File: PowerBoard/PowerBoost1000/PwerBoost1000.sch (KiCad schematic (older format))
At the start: 23 parts, among them T401 MMUN2133LT1G, U401 TPS61030RSAR

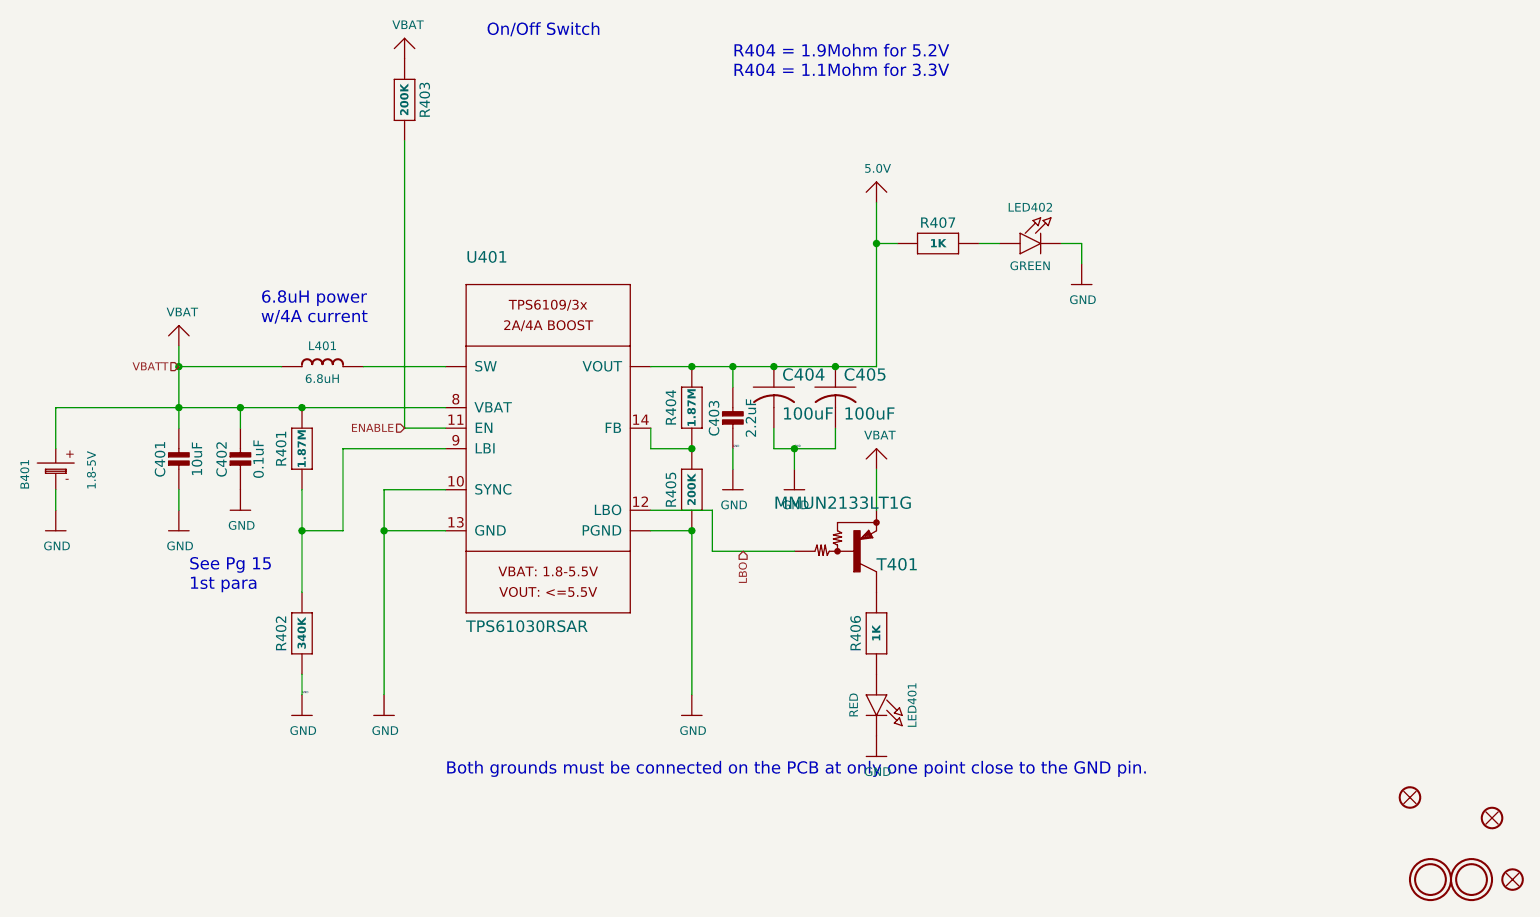
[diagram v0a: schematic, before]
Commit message: Replacing the SEPIC converter.
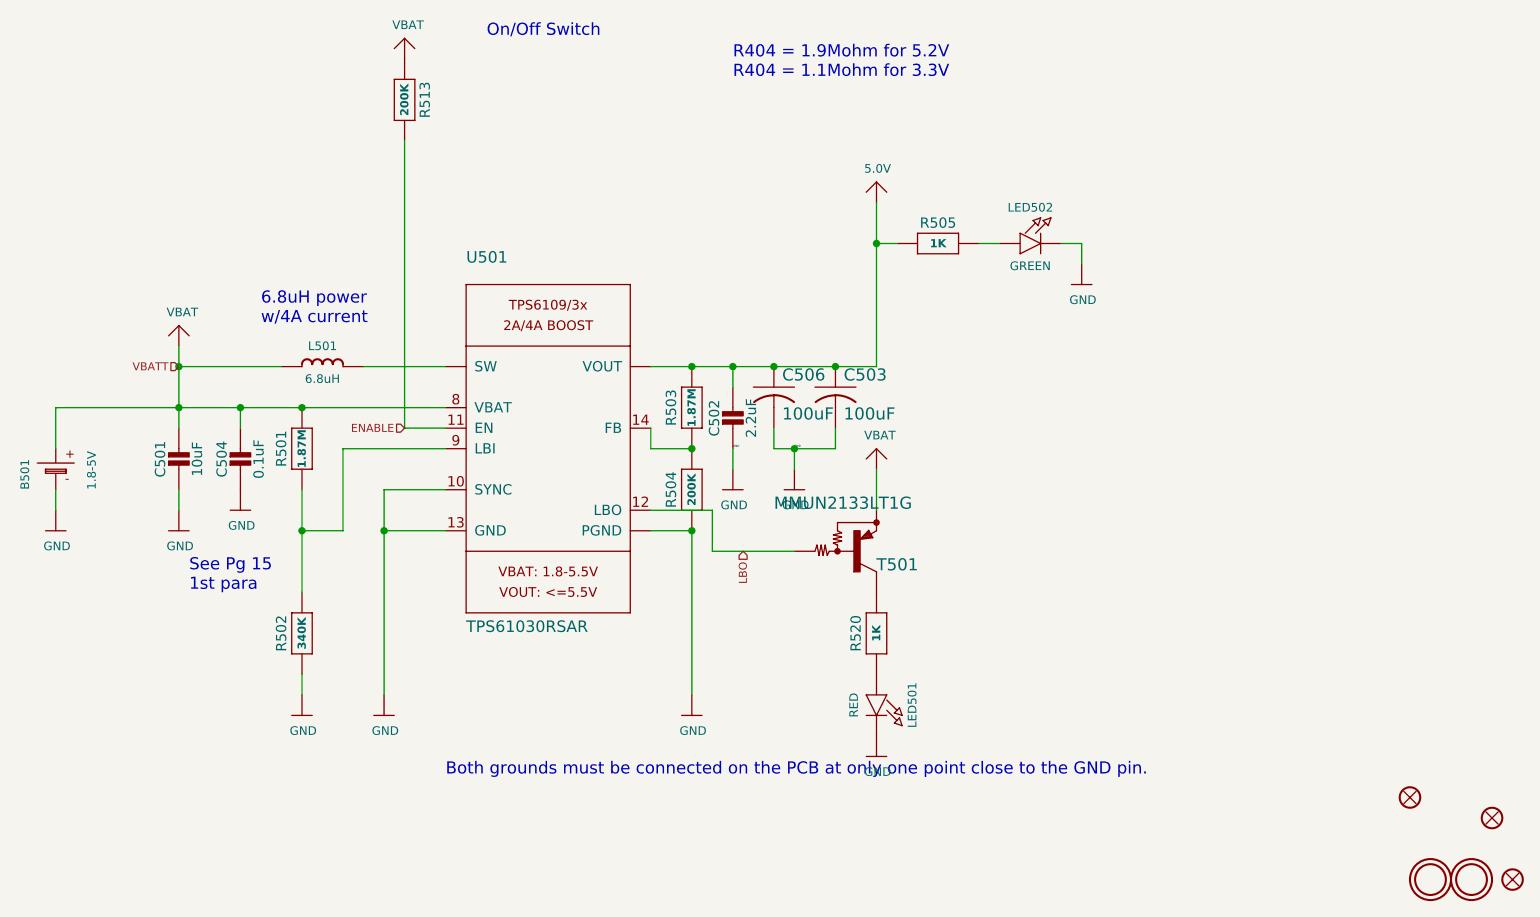
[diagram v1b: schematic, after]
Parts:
- C501: renamed from C401; footprint PowerBoost1000:0805-NO -> Capacitor_SMD:C_0805_2012Metric_Pad1.15x1.40mm_HandSolder
- C502: renamed from C403; footprint PowerBoost1000:0805-NO -> Capacitor_SMD:C_0805_2012Metric_Pad1.15x1.40mm_HandSolder
- C503: renamed from C405; footprint PowerBoost1000:C1210 -> Capacitor_SMD:C_1210_3225Metric_Pad1.42x2.65mm_HandSolder
- C504: renamed from C402; footprint PowerBoost1000:0805-NO -> Capacitor_SMD:C_0805_2012Metric_Pad1.15x1.40mm_HandSolder
- C506: renamed from C404; footprint PowerBoost1000:C1210 -> Capacitor_SMD:C_1210_3225Metric_Pad1.42x2.65mm_HandSolder
- R502: renamed from R402; footprint PowerBoost1000:_0805MP -> Resistor_SMD:R_0805_2012Metric_Pad1.15x1.40mm_HandSolder
- R503: renamed from R404; footprint PowerBoost1000:_0805MP -> Resistor_SMD:R_0805_2012Metric_Pad1.15x1.40mm_HandSolder
- R504: renamed from R405; footprint PowerBoost1000:0805-NO -> Resistor_SMD:R_0805_2012Metric_Pad1.15x1.40mm_HandSolder
- R505: renamed from R407; footprint PowerBoost1000:0805-NO -> Resistor_SMD:R_0805_2012Metric_Pad1.15x1.40mm_HandSolder
- R513: renamed from R403; footprint PowerBoost1000:0805-NO -> Resistor_SMD:R_0805_2012Metric_Pad1.15x1.40mm_HandSolder
- R520: renamed from R406; footprint PowerBoost1000:0805-NO -> Resistor_SMD:R_0805_2012Metric_Pad1.15x1.40mm_HandSolder
- U$501: renamed from U$401; footprint PowerBoost1000:MOUNTINGHOLE_2.5_PLATED -> MountingHole:MountingHole_2.5mm_Pad
- U$502: renamed from U$402; footprint PowerBoost1000:MOUNTINGHOLE_2.5_PLATED -> MountingHole:MountingHole_2.5mm_Pad
- U501: renamed from U401; footprint PowerBoost1000:PVQFN-16 -> Package_DFN_QFN:Texas_S-PVQFN-N16_EP2.7x2.7mm_ThermalVias
- renumbered B401 to B501, FID401 to FID501, FID402 to FID502, FID403 to FID503, L401 to L501, LED401 to LED501, LED402 to LED502, R401 to R501, T401 to T501
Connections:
- net GND: no longer R502.1

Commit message: Separating the power board branch.
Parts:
- removed B501: 1.8-5V, PowerBoost1000:JSTPH2, symbol PowerBoost1000-eagle-import:BATTERY
- removed L501: 6.8uH, PowerBoost1000:INDUCTOR_8X8MM, symbol PowerBoost1000-eagle-import:INDUCTOR-8X8
- removed LED501: RED, PowerBoost1000:CHIPLED_0805_NOOUTLINE, symbol PowerBoost1000-eagle-import:LED0805_NOOUTLINE
- removed LED502: GREEN, PowerBoost1000:CHIPLED_0805_NOOUTLINE, symbol PowerBoost1000-eagle-import:LED0805_NOOUTLINE
- removed R505, R520: 1K, Resistor_SMD:R_0805_2012Metric_Pad1.15x1.40mm_HandSolder, symbol PowerBoost1000-eagle-import:RESISTOR0805_NOOUTLINE
- removed T501: MMUN2133LT1G, PowerBoost1000:SC59-BEC, symbol PowerBoost1000-eagle-import:-PNP_DRIVER-SC59-BEC
- added L401: 6.8uH, PowerBoard:IND_B952AS-H-220M=P3, symbol PowerBoth-rescue:B952AS-H-220M=P3-PowerBoard-eagle-import
- C401: renamed from C501; DigiKey (none) -> EMK212BB7106MG-T; LCSC Part Number (none) -> C15850
- C402: renamed from C502; DigiKey (none) -> GRM21BR71C225KA12L; LCSC Part Number (none) -> C49217
- C403: renamed from C503; DigiKey (none) -> EMK325ABJ107MM-T
- C404: renamed from C504; DigiKey (none) -> C0805C104M3RACTU; LCSC Part Number (none) -> C49678
- C406: renamed from C506; DigiKey (none) -> EMK325ABJ107MM-T
- R401: renamed from R501; footprint PowerBoost1000:_0805MP -> Resistor_SMD:R_0805_2012Metric_Pad1.15x1.40mm_HandSolder; DigiKey (none) -> ERJ-6ENF1874V
- R402: renamed from R502; DigiKey (none) -> RC0805FR-07340KL; LCSC Part Number (none) -> C17636
- R403: renamed from R503; DigiKey (none) -> ERJ-6ENF1874V
- R404: renamed from R504; DigiKey (none) -> RMCF0805FT200K; LCSC Part Number (none) -> C17539
- R413: renamed from R513; DigiKey (none) -> RMCF0805FT200K; LCSC Part Number (none) -> C17539
- U401: renamed from U501; footprint Package_DFN_QFN:Texas_S-PVQFN-N16_EP2.7x2.7mm_ThermalVias -> PowerBoost1000:PVQFN-16; DigiKey (none) -> TPS61030RSAR; LCSC Part Number (none) -> C10110
- renumbered FID501 to FID401, FID502 to FID402, FID503 to FID403, U$501 to U$401, U$502 to U$402
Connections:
- net labels added: FromBoost
- net labels removed: 5.0V, VBAT
- wire segments 51 -> 49

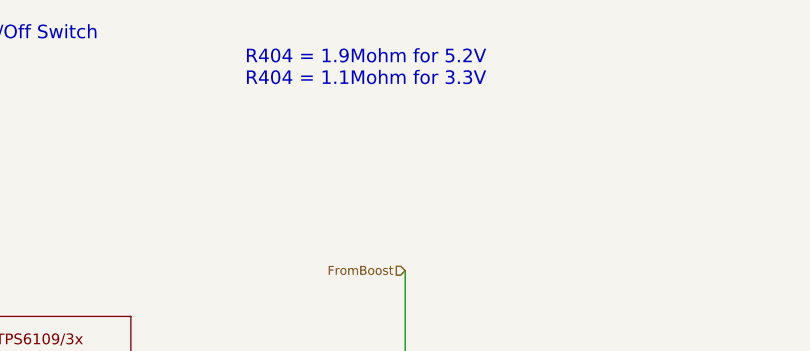
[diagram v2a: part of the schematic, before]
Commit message: The layout is not optimal for the PB and two capacitor values for the buck are incorrect.
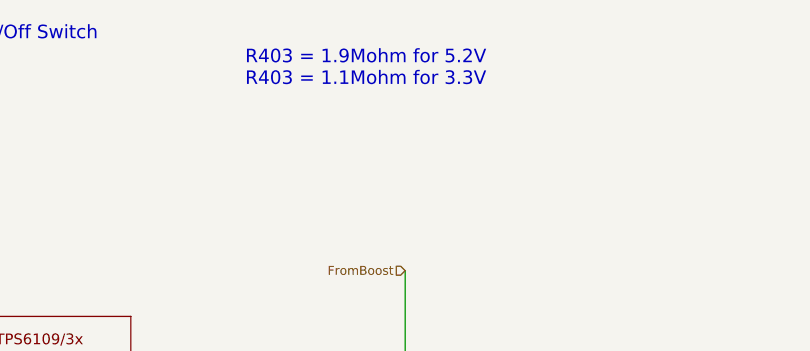
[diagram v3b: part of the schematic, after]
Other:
- note added: "R403 = 1.9Mohm for 5.2V\nR403 = 1.1Mohm for 3.3V"
- note removed: "R404 = 1.9Mohm for 5.2V\nR404 = 1.1Mohm for 3.3V"
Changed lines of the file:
@@
 6.8uH power\nw/4A current
 Text Notes 5600 1850 0    59   ~ 0
-R404 = 1.9Mohm for 5.2V\nR404 = 1.1Mohm for 3.3V
+R403 = 1.9Mohm for 5.2V\nR403 = 1.1Mohm for 3.3V
 Text HLabel 5900 4150 2    39   Input ~ 0
 LBO

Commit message: Buck/boost v4.0.
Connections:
- net labels added: FB, GNDPWR, LBI, SW
- wire segments 49 -> 51
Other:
- moved on the sheet: C402, C403, C406, R403, R404, R413
